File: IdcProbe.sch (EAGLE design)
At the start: 51 parts, among them IC1 TL074D, J2 BNCPTH, X1 MSTBA2, X2 MSTBA2

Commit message: work
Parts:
- removed H1, H2, H3, H4: MOUNT-PAD-ROUND3.2, holes:MOUNT-PAD-ROUND3.2
- removed J2: BNCPTH, SparkFun-Connectors:BNCPTH
- added C19, C31, C32: 4.7uF, rcl:C-EUC0805
- added C20: 100nF, rcl:C-EUC0805
- added C21: 6.8pF, rcl:C-EUC0805
- added C22, C23, C28, C29, C33, C34, C35, C36: 10uF, rcl:C-EUC1206
- added C25: 10nF, rcl:C-EUC0805
- added C26: 4.7nF, rcl:C-EUC0805
- added C27: 220nF, rcl:C-EUC0805
- added C30: 7.5pF, rcl:C-EUC0805
- added CN1: (no value), microbuilder:USBMINIBLARGE
- added D2, D3, D4: MBR0520, diode:DIODE-SOD123
- added L1, L2: 3.3uH, Jeroen:INDUCTOR_VLS3015
- added L3, L4: extra 3.3uH, Jeroen:INDUCTOR_VLS3015
- added LD1, LD2, LD3: (no value), led:LEDCHIP-LED0805
- added P1, P2: BANANA_SOCKETVERTICAL, Jeroen:BANANA_SOCKETVERTICAL
- added R12, R2: 10k, rcl:R-EU_R0805I
- added R13: 100, rcl:R-EU_R0805I
- added R14, R17: 1000k, rcl:R-EU_R0805I
- added R15, R16: 100k, rcl:R-EU_R0805I
- added R18, R19: 3.9k, rcl:R-EU_R0805I
- added R20: 1.5k, rcl:R-EU_R0805I
- added TP1: V+, Jeroen:TESTPOINT
- added TP10, TP12, TP2, TP3, TP7: TESTPOINT_GND, Jeroen:TESTPOINT_GND
- added U$1: PCB_HAMMOND_1591XXL, Jeroen:PCB_HAMMOND_1591XXL
- added U2: TPS65131RGET, Jeroen:TPS65131RGET
- added X3: R141426, con-coax:R141426
- added X4: MSTBA2, con-phoenix-508:MSTBA2
- PS1: device Jeroen:RX_XXXXDRP -> Jeroen:RX_XXXXDRD
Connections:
- new net CN: C26.1, U2.CN
- new net CP: C25.1, U2.CP
- new net FBN: C30.1, R16.1, R17.1, U2.FBN
- new net FBP: C21.2, R14.1, R15.2, U2.FBP
- new net INP: D2.A, L1.2, U2.INP, U2.INP_2
- new net N$12: LD3.A, R19.2
- new net N$13: IC1A.-IN, R12.2, R2.1
- new net N$14: CN1.VBUS, D4.A, X4-1.1
- new net N$15: LD1.A, R20.1
- new net N$4: LD2.A, R18.1
- new net OUTN: D3.C, L2.2, U2.OUTN, U2.OUTN_2
- new net RV+: C21.1, C22.1, C33.1, D2.C, L4.1, R14.2, TP2.P$1, U2.VPOS
- new net RV-: C23.1, C30.2, C35.1, D3.A, L3.1, R17.2, TP12.P$1, U2.VNEG
- new net VI: C19.1, C31.1, C32.1, D4.C, L1.1, R13.2, R20.2, TP7.P$1, U2.INN, U2.INN_2
- new net VIN1: C20.1, R13.1, U2.ENN, U2.ENP, U2.PSN, U2.PSP, U2.VIN
- new net VREF: C27.1, R16.2, U2.VREF
- net GND: now also C14.+, C19.2, C20.2, C22.2, C23.2, C25.2, C26.2, C27.2, C28.2, C29.2, C31.2, C32.2, C33.2, C34.2, C35.2, C36.2, CN1.GND, L2.1, LD1.C, LD2.C, LD3.C, R12.1, R15.1, TP1.P$1, TP10.P$2, TP12.P$2, TP2.P$2, TP3.P$2, TP7.P$2, U2.AGND, U2.EP, U2.PGND, U2.PGND_2, X3.2, X4-2.1; no longer C14.-, J2.GND
- net N$1: now also X3.1; no longer J2.OUT
- net N$2: now also P1.A
- net N$3: now also P2.A
- net N$9: now also R2.2; no longer IC1A.-IN
- net V+: now also C29.1, C34.1, L4.2, R18.2, TP3.P$1
- net V-: now also C14.-, C28.1, C36.1, L3.2, R19.1, TP10.P$1; no longer C14.+
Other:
- note added: "Equations VNEG: vn = ( vref * (r1 * r2) / r2 ) vn = ( 1.213 * (1000 * 100) / 100 ) vn = -13.43"
- note added: "Equations VPOS: r1 = r2 * (vp/vref-1) vp = ( vref * (r1 * r2) / r2 ) vp = ( 2.213 * (1000 * 100) / 100 ) vp = 12.13"
- note added: "SRN3010"
- note added: "should be 22uF"

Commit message: update
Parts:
- removed C27: 220nF, rcl:C-EUC0805
- removed C28, C29, C33, C34, C35, C36: 10uF, rcl:C-EUC1206
- removed C30: 7.5pF, rcl:C-EUC0805
- removed C31, C32: 4.7uF, rcl:C-EUC0805
- removed CN1: (no value), microbuilder:USBMINIBLARGE
- removed D1: SS24A, diode:DIODE-DO-214AC
- removed D4: MBR0520, diode:DIODE-SOD123
- removed LD1: (no value), led:LEDCHIP-LED0805
- removed PS1: RP-1215D, Jeroen:RX_XXXXDRD
- removed R1: 240, rcl:R-EU_R0805
- removed R15, R16: 100k, rcl:R-EU_R0805I
- removed R17: 1000k, rcl:R-EU_R0805I
- removed R18, R19: 3.9k, rcl:R-EU_R0805I
- removed R20: 1.5k, rcl:R-EU_R0805I
- removed TP10, TP12, TP3: TESTPOINT_GND, Jeroen:TESTPOINT_GND
- removed TP11, TP15, TP6: GND, Jeroen:TESTPOINT
- removed TP13: +15V, Jeroen:TESTPOINT
- removed TP14: V+, Jeroen:TESTPOINT
- removed VREG1: VREG_3PINS_ADJ-LM317T-TO-220VA, dp_devices:VREG_3PINS_ADJ-LM317T-TO-220VA
- removed VREG2: VREG_3PINS_ADJ-LM337T-TO-220VB, dp_devices:VREG_3PINS_ADJ-LM337T-TO-220VB
- removed X1, X2, X4: MSTBA2, con-phoenix-508:MSTBA2
- added J1: (no value), SparkFun-Connectors:CONN_02POLAR
- C1, C3: value 100nF -> 4.7uF
- C10: value 100nF -> 6.8pF
- C11, C12: value 100nF -> 10uF; device rcl:C-EUC0805 -> rcl:C-EUC1206
- C13, C14: value 47uF -> 10uF; device rcl:CPOL-EUD -> rcl:C-EUC1206
- C15: value 3.3nF -> 10uF; device rcl:C-EUC0805 -> rcl:C-EUC1206
- C16, C17: value (none) -> 10uF; device rcl:C-EUC0805 -> rcl:C-EUC1206
- C18: value (none) -> 100nF
- C19: value 4.7uF -> 100nF
- C2: value 10uF -> 4.7uF; device rcl:C-EUC1206 -> rcl:C-EUC0805
- C21: value 6.8pF -> 47uF; device rcl:C-EUC0805 -> rcl:CPOL-EUD
- C22: value 10uF -> 47uF; device rcl:C-EUC1206 -> rcl:CPOL-EUD
- C23: value 10uF -> 3.3nF; device rcl:C-EUC1206 -> rcl:C-EUC0805
- C24: value 100nF -> (none)
- C25: value 10nF -> (none)
- C26: value 4.7nF -> (none)
- C4: value 2.2uF -> 100nF
- C5: value 1uF -> 10nF
- C6: value 100nF -> 4.7nF
- C7: value 10uF -> 220nF; device rcl:C-EUC1206 -> rcl:C-EUC0805
- C8: value 100nF -> 7.5pF
- C9: value 2.2uF -> 10uF; device rcl:C-EUC0805 -> rcl:C-EUC1206
- R10: value 240 -> (none)
- R11: value 10k -> (none)
- R12: device rcl:R-EU_R0805I -> rcl:R-EU_R0805
- R13: value 100 -> 10k
- R14: value 1000k -> 10k
- R2: value 10k -> 100
- R3, R6: value 2.2k -> 100k; device rcl:R-EU_R0805 -> rcl:R-EU_R0805I
- R4: value (none) -> 1000k; device rcl:R-EU_R0805 -> rcl:R-EU_R0805I
- R5: value 15 -> 1000k; device rcl:R-EU_R0805 -> rcl:R-EU_R0805I
- R7: value (none) -> 3.9k; device rcl:R-EU_R0805 -> rcl:R-EU_R0805I
- R8: value 33k -> 3.9k; device rcl:R-EU_R0805 -> rcl:R-EU_R0805I
- R9: value 33k -> 15
- TP1, TP4: value V+ -> (none)
- TP5: value GND -> TESTPOINT_GND; device Jeroen:TESTPOINT -> Jeroen:TESTPOINT_GND
- TP8: value V- -> (none)
- TP9: value -15V -> TESTPOINT_GND; device Jeroen:TESTPOINT -> Jeroen:TESTPOINT_GND
- U1: value (none) -> TPS65131RGET; device Jeroen:CMS3005 -> Jeroen:TPS65131RGET
- U2: value TPS65131RGET -> (none); device Jeroen:TPS65131RGET -> Jeroen:CMS3005
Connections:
- removed net +15V: C1.2, C2.2, PS1.+VOUT, TP13.P$1, VREG1.VIN
- removed net -15V: C6.1, C7.1, PS1.-VOUT, TP9.P$1, VREG2.VIN
- removed net N$15 (its old number): LD1.A, R20.1
- removed net N$3: P2.A, U1.OUT, X2-1.1
- removed net N$38: D1.A, X1-1.1
- removed net N$4: LD2.A, R18.1
- removed net N$40: R1.2, R3.2, R8.2, VREG1.ADJ
- removed net N$42: R10.2, R6.1, R9.1, VREG2.ADJ
- removed net N$7 (its old number): C15.2, R5.2
- removed net N$8 (its old number): C17.2, R4.2
- removed net PGND: C24.2, C5.2, PS1.-VIN, X1-2.1
- removed net PWR_VIN: C24.1, C5.1, D1.C, PS1.+VIN
- removed net VIN1: C20.1, R13.1, U2.ENN, U2.ENP, U2.PSN, U2.PSP, U2.VIN
- new net N$11: IC1A.OUT, R11.1, R12.2, R13.2
- new net N$5: P1.A, U2.IN
- new net N$6: P2.A, U2.OUT
- new net VIN: C4.1, R2.1, U1.ENN, U1.ENP, U1.PSN, U1.PSP, U1.VIN
- net CN: now also C6.1, U1.CN; no longer C26.1, U2.CN
- net CP: now also C5.1, U1.CP; no longer C25.1, U2.CP
- net FBN: now also C8.1, R3.1, R4.1, U1.FBN; no longer C30.1, R16.1, R17.1, U2.FBN
- net FBP: now also C10.2, R5.1, R6.2, U1.FBP; no longer C21.2, R14.1, R15.2, U2.FBP
- net GND: now also C1.2, C11.2, C12.2, C13.2, C14.2, C15.2, C16.2, C17.2, C19.1, C2.2, C20.1, C21.-, C22.+, C23.1, C24.1, C25.1, C26.1, C3.2, C4.2, C5.2, J1.1, R14.1, R6.1, TP5.P$2, TP8.P$1, TP9.P$2, U1.AGND, U1.EP, U1.PGND, U1.PGND_2, U2.GND, U2.SGND; no longer C1.1, C11.1, C12.1, C13.-, C14.+, C15.1, C16.1, C17.1, C18.1, C19.2, C2.1, C20.2, C22.2, C23.2, C25.2, C26.2, C27.2, C28.2, C29.2, C3.1, C31.2, C32.2, C33.2, C34.2, C35.2, C36.2, C4.1, C8.2, CN1.GND, LD1.C, PS1.COM, R11.1, R15.1, R3.1, R6.2, R8.1, R9.2, TP10.P$2, TP11.P$1, TP12.P$2, TP15.P$1, TP3.P$2, TP6.P$1, U1.GND, U1.SGND, U2.AGND, U2.EP, U2.PGND, U2.PGND_2, X4-2.1
- net INP: now also U1.INP, U1.INP_2; no longer U2.INP, U2.INP_2
- net N$1: now also LD2.A, R7.1; no longer C18.2, R7.2, TP5.P$1, X3.1
- net N$10: now also C25.2, R10.2; no longer C16.2, IC1A.+IN, R4.1, R5.1, U1.VOUT
- net N$12: now also C26.2, R11.2, TP9.P$1, X3.1; no longer LD3.A, R19.2
- net N$13: now also C24.2, IC1A.+IN, R10.1, R9.1, TP7.P$1, U2.VOUT; no longer IC1A.-IN, R12.2, R2.1
- net N$14: now also IC1A.-IN, R13.1, R14.2; no longer CN1.VBUS, D4.A, X4-1.1
- net N$2: now also LD3.A, R8.2; no longer P1.A, U1.IN, X2-2.1
- net N$9: now also C23.2, R9.2; no longer IC1A.OUT, R11.2, R2.2, R7.1
- net OUTN: now also U1.OUTN, U1.OUTN_2; no longer U2.OUTN, U2.OUTN_2
- net RV+: now also C10.1, C11.1, C14.1, R5.2, U1.VPOS; no longer C21.1, C22.1, C33.1, R14.2, TP2.P$1, U2.VPOS
- net RV-: now also C16.1, C8.2, C9.1, R4.2, U1.VNEG; no longer C23.1, C30.2, C35.1, R17.2, TP12.P$1, U2.VNEG
- net V+: now also C13.1, C15.1, C18.2, C19.2, C21.+, R7.2, TP2.P$1, U2.+; no longer C10.2, C11.2, C13.+, C29.1, C3.2, C34.1, C4.2, R1.1, R18.2, TP14.P$1, TP3.P$1, U1.+, VREG1.VOUT
- net V-: now also C12.1, C17.1, C18.1, C20.2, C22.-, R8.1, TP5.P$1, U2.-; no longer C10.1, C12.2, C14.-, C28.1, C36.1, C8.1, C9.1, R10.1, R19.1, TP10.P$1, TP8.P$1, U1.-, VREG2.VOUT
- net VI: now also C1.1, C2.1, C3.1, J1.2, R2.2, U1.INN, U1.INN_2; no longer C19.1, C31.1, C32.1, D4.C, R13.2, R20.2, TP7.P$1, U2.INN, U2.INN_2
- net VREF: now also C7.1, R3.2, U1.VREF; no longer C27.1, R16.2, U2.VREF
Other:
- note added: "5V input"
- note removed: "12 Volt nominal 10.8 to 13.2 Volt"
- note removed: "R1"
- note removed: "R2"
- note removed: "RP-1215D Unregulated ±15 Volt (5% 14.25-15.75) 66 mA max (470 uF)"
- note removed: "VOUT = 1.25 * ( 1 + R2/R1 ) 1.25 * (1 + 3330 / 560 ) = 8.6 V With regulator bypass 2046"

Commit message: work
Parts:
- removed C15, C17: 10uF, rcl:C-EUC1206
- removed U2: (no value), Jeroen:CMS3005
- added D6: SS24 (40V), microbuilder:DIODESMA
- added LED1: (no value), led:LED3MM
- added R1: 1K, rcl:R-EU_R0805
- added R15: 2M, rcl:R-EU_R0805
- added R16: 100k, Jeroen:POT_MULTI
- added R17: 100, rcl:R-EU_R0805I
- added U3: (no value), Jeroen:CMS3000_15A
- R11: value (none) -> 0
- R12: value 10k -> 100k
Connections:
- new net N$16: LED1.A, R17.1
- new net N$3: IC1A.+IN, IC1B.OUT, R1.2
- new net N$4: IC1B.-IN, R1.1, R15.2
- net GND: now also D6.A, LED1.C, U3.GND, U3.SGND; no longer C15.2, C17.2, IC1B.+IN, U2.GND, U2.SGND
- net N$13: now also IC1B.+IN, U3.VOUT; no longer IC1A.+IN, U2.VOUT
- net N$15: now also R15.1, R16.SW; no longer IC1B.-IN, IC1B.OUT
- net N$5: now also U3.IN; no longer U2.IN
- net N$6: now also U3.OUT; no longer U2.OUT
- net V+: now also R16.CW, R17.2, U3.+; no longer C15.1, U2.+
- net V-: now also R16.CCW, U3.-; no longer C17.1, U2.-
- net VI: now also D6.C
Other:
- note added: "Multiply to 1V/A gain"
- note added: "Offset correct"
- note added: "Ra"
- note added: "Range: +-V * (Ra/Rb) 24 * (1k/2M) 0.012V"
- note added: "Rb"
- moved on the sheet: C1, C19, C2, C20, C21, C22, C23, C24, C25, C26, C3, C4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

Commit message: Update smps
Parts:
- removed D3: MBR0520, diode:DIODE-SOD123
- removed D6: SS24 (40V), microbuilder:DIODESMA
- removed TP2, TP5: TESTPOINT_GND, Jeroen:TESTPOINT_GND
- added C15, C17, C27, C28: 4.7uF 25V X5R, rcl:C-EUC0805
- added C29, C30: 100nF, rcl:C-EUC0805
- added D1, D4: PMEG4010BEA, diode:DIODE-SOD323-R
- added D5: SMAJ5.0A, Jeroen:SMAJ13A-TR
- added F1: PTC Ih 0.5, dp_devices:FUSE_PTC-0805
- added R18, R19: 10k, rcl:R-EU_R0805I
- C1, C2, C3: value 4.7uF -> 4.7uF 25V X5R
- C11, C12, C13, C14, C16, C9: value 10uF -> 4.7uF 25V X5R; device rcl:C-EUC1206 -> rcl:C-EUC0805
- C5: value 10nF -> 10nF 16V X7R
- C6: value 4.7nF -> 4.7nF 50V C0G
- D2: value MBR0520 -> PMEG4010BEA; device diode:DIODE-SOD123 -> diode:DIODE-SOD323-R
- L1, L2: value 3.3uH -> 2.2uH
- L3, L4: value extra 3.3uH -> 2.2uH
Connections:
- new net N$21: F1.1, J1.2
- net GND: now also C15.2, C17.2, C27.2, C28.2, C29.2, C30.2, D2.A, D5.A, R18.1, R19.2, U1.PSN, U1.PSP; no longer D6.A, TP2.P$2, TP5.P$2
- net INP: now also D4.A; no longer D2.A
- net OUTN: now also D1.C; no longer D3.C
- net RV+: now also C13.1, C15.1, D4.C; no longer D2.C
- net RV-: now also C17.1, C27.1, D1.A; no longer D3.A
- net V+: now also C12.1, R18.2; no longer C13.1, TP2.P$1
- net V-: now also C28.1, R19.1; no longer C12.1, TP5.P$1
- net VI: now also C29.1, C30.1, D2.C, D5.C, F1.2, U1.ENN, U1.ENP; no longer D6.C, J1.2
- net VIN: no longer U1.ENN, U1.ENP, U1.PSN, U1.PSP
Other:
- note added: "Base load"
- note added: "Booster"
- note added: "Disable power save mode"
- note added: "Enable Negative"
- note added: "Enable Positive"
- note added: "Extra filter"
- note added: "Inverter"
- note added: "Overvoltage"
- note added: "Polyfuse"
- note added: "Reverse polarity"
- note removed: "should be 22uF"
- moved on the sheet: C1, C10, C11, C12, C13, C14, C16, C2, C3, C4, C5, C6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

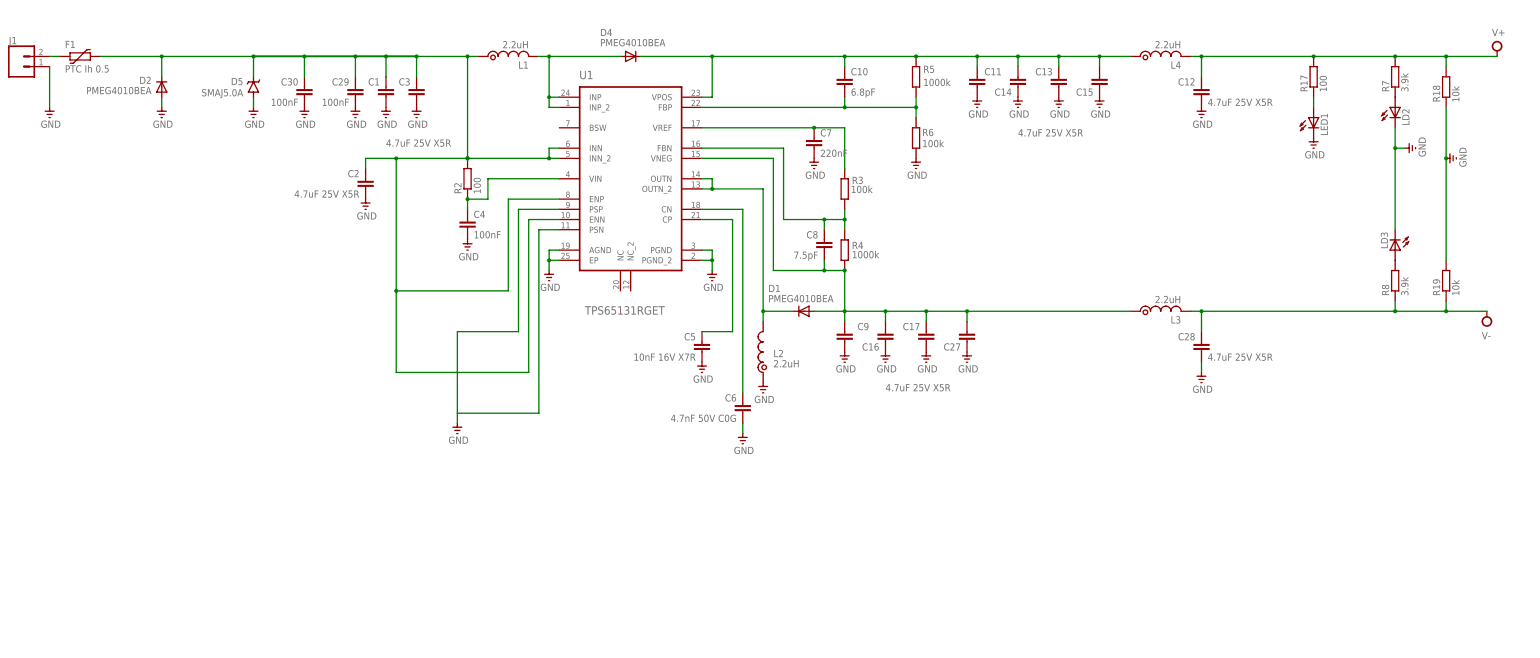
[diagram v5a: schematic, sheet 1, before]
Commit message: Update
- Update SMPS
- Add supply protection
- Add documentation
- Started with attributes for BOM.
- Added divide gain option
- Printed pdf and generated gerbers
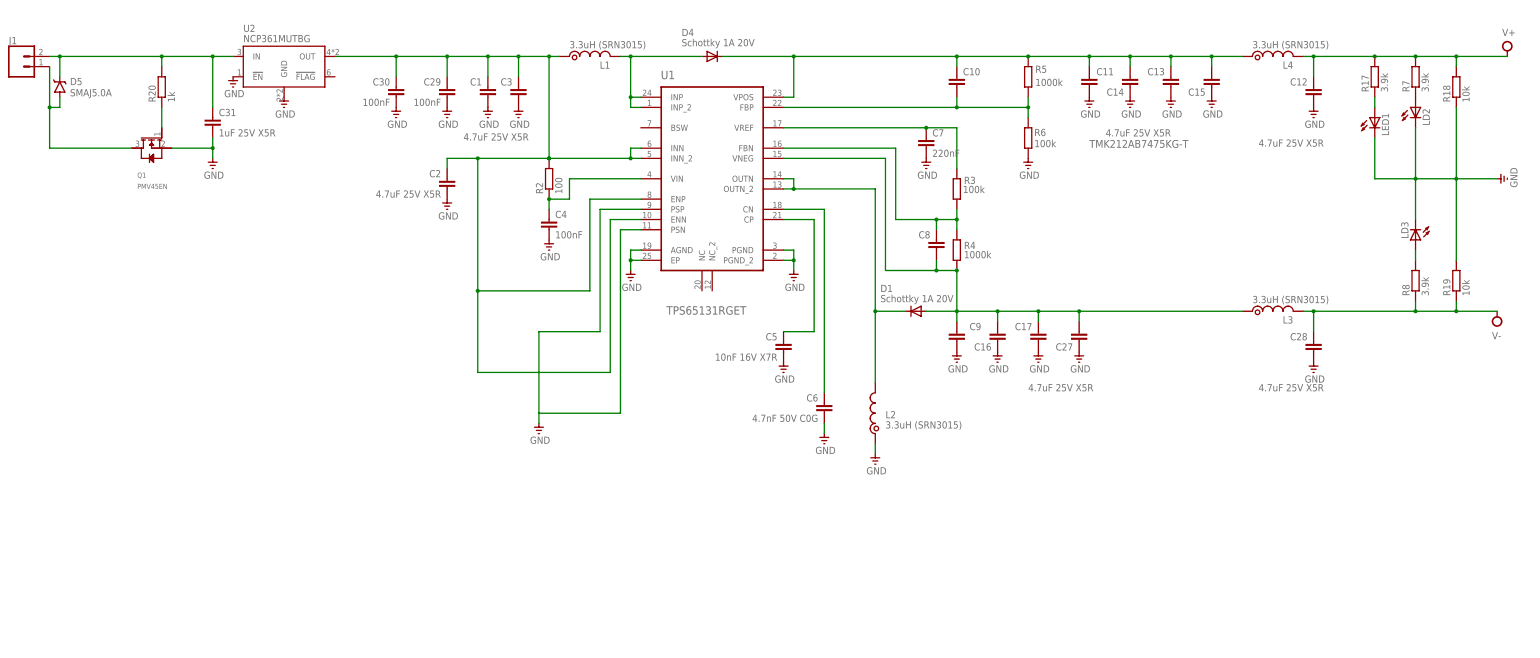
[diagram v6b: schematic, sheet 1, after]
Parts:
- removed D2: PMEG4010BEA, diode:DIODE-SOD323-R
- removed F1: PTC Ih 0.5, dp_devices:FUSE_PTC-0805
- added C31: 1uF 25V X5R, rcl:C-EUC0805
- added Q1: PMV45EN, Jeroen:PMV45EN
- added R20: 1k, rcl:R-EU_R0805I
- added R21: 10k, rcl:R-EU_R0805I
- added R22: (no value), rcl:R-EU_R0805I
- added U2: NCP361MUTBG, Jeroen:NCP36XMU
- C1, C11, C12, C13, C14, C15, C16, C17, C2, C27, C28, C3, C9, D5, J1: MPN (none) -> TMK212AB7475KG-T
- C10: value 6.8pF -> (none)
- C21, C22: value 47uF -> 47uF (EEEFK1V470P)
- C23: value 3.3nF -> 3.3nF / 2.2nF
- C8: value 7.5pF -> (none)
- D1, D4: value PMEG4010BEA -> Schottky 1A 20V; MPN (none) -> PMEG4010BEA
- L1, L2, L3, L4: value 2.2uH -> 3.3uH (SRN3015)
- R14: value 10k -> (none)
- R15: value 2M -> 1.8M
- R16: MPN (none) -> 3386P-1-104LF
- R17: value 100 -> 3.9k
- R9: value 15 -> 15 / 33
- renumbered IC1 to U4
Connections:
- removed net N$21: F1.1, J1.2
- new net N$17: C31.1, D5.C, J1.2, R20.2, U2.IN
- new net N$18: D5.A, J1.1, Q1.D
- new net N$19: Q1.G, R20.1
- new net N$20: R21.2, R22.2, U4A.+IN
- net GND: now also C31.2, Q1.S, R22.1, U2.!EN, U2.GND; no longer D2.A, D5.A, J1.1
- net N$3: now also R21.1; no longer U4A.+IN
- net VI: now also U2.OUT; no longer D2.C, D5.C, F1.2
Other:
- note added: "Clamp 7V"
- note added: "Depending on CMS3000 model CMS3005/CMS30015"
- note added: "Front panel LED"
- note added: "Indicator LED"
- note added: "NCP361: UVLO: 3.0 OVLO: 5.6"
- note added: "Option to divide to gain"
- note added: "Option to multiply gain"
- note added: "Overcurrent protection U2"
- note added: "Overvoltage protection U2"
- note added: "Q1 conditions: Vgs +-20V"
- note added: "Range: +-V * (Ra/Rb) 24 * (1k/1.8M) 0.013V"
- note added: "Reverse polarity protection Q1"
- note added: "Transient protection D5"
- note removed: "5V input"
- note removed: "Multiply to 1V/A gain"
- note removed: "Overvoltage"
- note removed: "Polyfuse"
- note removed: "Range: +-V * (Ra/Rb) 24 * (1k/2M) 0.012V"
- note removed: "Reverse polarity"
- note removed: "SRN3010"
- moved on the sheet: C1, C10, C11, C12, C13, C14, C15, C16, C17, C2, C26, C27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
